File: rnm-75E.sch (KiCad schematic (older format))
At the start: 200 parts, among them J1 AVR-ISP-6, J2 USB_C_Receptacle_USB2.0, SW1 SW_Push, SW2 Rotary_Encoder_Switch, U1 AT90USB646-AU, U2 ATmega32U4-AU, Y1 Crystal_GND24_Small

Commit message: update mcu
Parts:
- removed U2: ATmega32U4-AU, Package_QFP:TQFP-44_10x10mm_P0.8mm, symbol MCU_Microchip_ATmega:ATmega32U4-AU
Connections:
- wire segments 419 -> 417
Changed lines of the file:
@@
 D+1
-$Comp
-L MCU_Microchip_ATmega:ATmega32U4-AU U2
-U 1 1 609C8DFF
-P 8750 4550
-F 0 "U2" H 8450 3950 50  0000 C CNN
-F 1 "ATmega32U4-AU" H 8650 3800 50  0000 C CNN
-F 2 "Package_QFP:TQFP-44_10x10mm_P0.8mm" H 8750 4550 50  0001 C CIN
-F 3 "http://ww1.microchip.com/downloads/en/DeviceDoc/Atmel-7766-8-bit-AVR-ATmega16U4-32U4_Datasheet.pdf" H 8750 4550 50  0001 C CNN
-	1    8750 4550
-	1    0    0    -1
-$EndComp
 $Comp
 L Device:R_Small R_u1
@@
 	1    0    0    -1
 $EndComp
-Wire Wire Line
-	7100 6200 6800 6200
 $Comp
 L power:GND #PWR0115
@@
 Text GLabel 3850 4800 2    50   Input ~ 0
 MOSI
-Wire Wire Line
-	6600 6200 6150 6200
 Text GLabel 3850 4900 2    50   Input ~ 0
 MISO

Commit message: pcb arranged
diodes added
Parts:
- added CAPS_LOCK_LED1: LED, LED_SMD:LED_0805_2012Metric, symbol Device:LED
- added D89, D90, D91, D92, D93, D94, D95, D96, D97, D98: WS2812B, LED_SMD:LED_WS2812B_PLCC4_5.0x5.0mm_P3.2mm, symbol LED:WS2812B
- added J3: Conn_01x04, Connector_PinSocket_2.54mm:PinSocket_1x04_P2.54mm_Vertical, symbol Connector_Generic:Conn_01x04
- added R1: 500, Resistor_SMD:R_0805_2012Metric, symbol Device:R_Small
- CF3, C_F1, C_F2, C_F4, C_FM1, C_X1, C_X2, C_ucap1: footprint (none) -> Capacitor_SMD:C_0805_2012Metric
- D1, D10, D11, D12, D13, D14, D15, D16, D17, D18, D19, D2, D20, D21, D22, D23, D24, D25, D26, D27, D28, D29, D3, D30, D31, D32, D33, D34, D35, D36, D37, D38, D39, D4, D40, D41, D42, D43, D44, D45, D46, D47, D48, D49, D5, D50, D51, D52, D53, D54, D55, D56, D57, D58, D59, D6, D60, D61, D62, D63, D64, D65, D66, D67, D68, D69, D7, D70, D71, D72, D73, D74, D75, D76, D77, D78, D79, D8, D80, D81, D82, D83, D84, D85, D86, D87, D88, D9: footprint (none) -> Diode_SMD:D_SOD-123
- F1: footprint (none) -> Fuse:Fuse_1206_3216Metric
- J1: footprint (none) -> Connector_PinSocket_1.00mm:PinSocket_2x03_P1.00mm_Vertical_SMD
- J2: footprint (none) -> Connector_USB:USB_C_Receptacle_HRO_TYPE-C-31-M-12
- MX1, MX12, MX13, MX15, MX16, MX17, MX18, MX19, MX2, MX21, MX22, MX23, MX24, MX25, MX26, MX27, MX28, MX29, MX3, MX30, MX31, MX32, MX33, MX34, MX35, MX36, MX37, MX38, MX39, MX4, MX40, MX42, MX43, MX44, MX45, MX46, MX47, MX48, MX49, MX5, MX50, MX51, MX52, MX53, MX54, MX55, MX56, MX57, MX58, MX59, MX6, MX60, MX61, MX62, MX63, MX65, MX66, MX67, MX68, MX69, MX7, MX70, MX72, MX73, MX74, MX75, MX76, MX78, MX79, MX83, MX84, MX85, MX86, MX87, MX88, MX89: footprint (none) -> MX_ONLY:MXOnly-1U-NoLED
- MX10, MX82: footprint (none) -> MX_ONLY:MXOnly-2.25U-NoLED
- MX11, MX14, MX20: footprint (none) -> MX_ONLY:MXOnly-1.25U-NoLED
- MX41: footprint (none) -> MX_ONLY:MXOnly-6.25U-ReversedStabilizers-NoLED
- MX64, MX71, MX8, MX81: footprint (none) -> MX_ONLY:MXOnly-1.5U-NoLED
- MX77, MX9: footprint (none) -> MX_ONLY:MXOnly-1.75U-NoLED
- MX80: footprint (none) -> MX_ONLY:MXOnly-2U-NoLED
- R_SW1, R_SW2, R_d1, R_d2, R_u1, R_u2: footprint (none) -> Resistor_SMD:R_0805_2012Metric
- SW1: footprint (none) -> random_keyboard_parts:SKQG-1155865
- SW2: footprint (none) -> Rotary_Encoder:RotaryEncoder_Alps_EC12E-Switch_Vertical_H20mm
- Y1: footprint (none) -> Crystal:Crystal_SMD_3225-4Pin_3.2x2.5mm
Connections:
- net +5V: now also SW2.A, SW2.B, U1.1 (PE6), U1.2 (PE7), D89.1 (VDD), D90.1 (VDD), D91.1 (VDD), D92.1 (VDD), D93.1 (VDD), D94.1 (VDD), D95.1 (VDD), D96.1 (VDD), D97.1 (VDD), D98.1 (VDD)
- net COL0: now also SW2.S1
- net COL10: no longer MX64.1 (COL)
- net COL15: no longer SW2.S1
- net COL7: now also U1.51 (PA0)
- net COL9: now also MX64.1 (COL)
- net GND: now also SW2.C, D89.3 (VSS), D90.3 (VSS), D91.3 (VSS), D92.3 (VSS), D93.3 (VSS), D94.3 (VSS), D95.3 (VSS), D96.3 (VSS), D97.3 (VSS), D98.3 (VSS), J3.4 (Pin_4), R1.2
- net ROWA: now also U1.32 (PD7); no longer U1.30 (PD5)
- net ROWB: now also U1.31 (PD6); no longer U1.29 (PD4)
- net ROWC: now also U1.30 (PD5); no longer U1.28 (PD3)
- net ROWD: now also U1.29 (PD4); no longer U1.27 (PD2)
- net ROWE: now also U1.28 (PD3); no longer U1.26 (PD1)
- net ROWF: now also U1.27 (PD2); no longer U1.25 (PD0)
- net VCC: now also J3.3 (Pin_3)
- net at D60.2 (A), MX63.2 (ROW): no longer MX64.2 (ROW)
- net at D53.2 (A), MX53.2 (ROW): now also MX64.2 (ROW)
- net LED_PIN: now reaches U1.10 (PB0)
- net LED_PIN: now also CAPS_LOCK_LED1.2 (A)
- net LED: now reaches U1.9 (PE3)
- net LED: now also D89.4 (DIN)
- new net: D89.2 (DOUT), D90.4 (DIN)
- new net: D90.2 (DOUT), D91.4 (DIN)
- new net: D91.2 (DOUT), D92.4 (DIN)
- new net: D92.2 (DOUT), D93.4 (DIN)
- new net: D93.2 (DOUT), D94.4 (DIN)
- new net: D94.2 (DOUT), D95.4 (DIN)
- new net: D95.2 (DOUT), D96.4 (DIN)
- new net: D96.2 (DOUT), D97.4 (DIN)
- new net: D97.2 (DOUT), D98.4 (DIN)
- new net: CAPS_LOCK_LED1.1 (K), R1.1
- new net SCL: J3.2 (Pin_2), U1.25 (PD0)
- new net SDA: J3.1 (Pin_1), U1.26 (PD1)
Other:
- note added: "LED TAP IN AFTER FUSE\n"
- moved on the sheet: D1, D10, D11, D12, D13, D14, D15, D16, D17, D18, D19, D2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

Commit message: stepped caps_lock
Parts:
- added MX90: MX-NoLED, MX_ONLY:MXOnly-1.25U-NoLED, symbol MX_ALPS_HYBRID:MX-NoLED
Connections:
- net COL1: now also MX90.1 (COL)
- net at D9.2 (A), MX9.2 (ROW): now also MX90.2 (ROW)
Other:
- note added: "ADD STEPPED CAPS SUPPORT\nUSES STEM PLACEMENT INLINE WITH L-CTRL\n"
- moved on the sheet: CAPS_LOCK_LED1, CF3, C_F1, C_F2, C_F4, C_FM1, C_X1, C_X2, C_ucap1, D1, D10, D11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

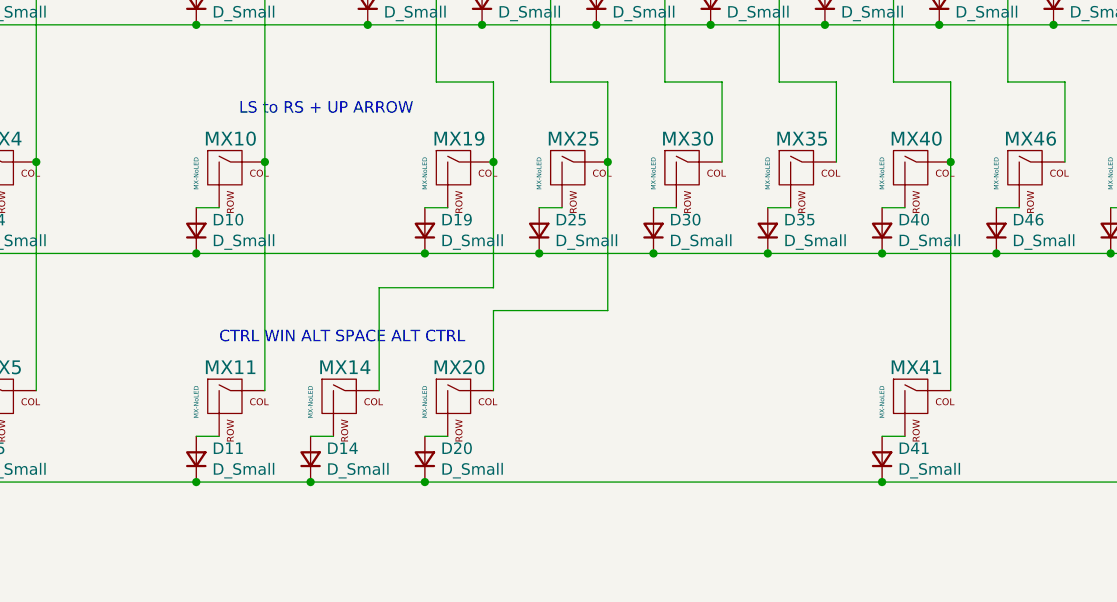
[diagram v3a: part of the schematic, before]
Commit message: added 7u space support
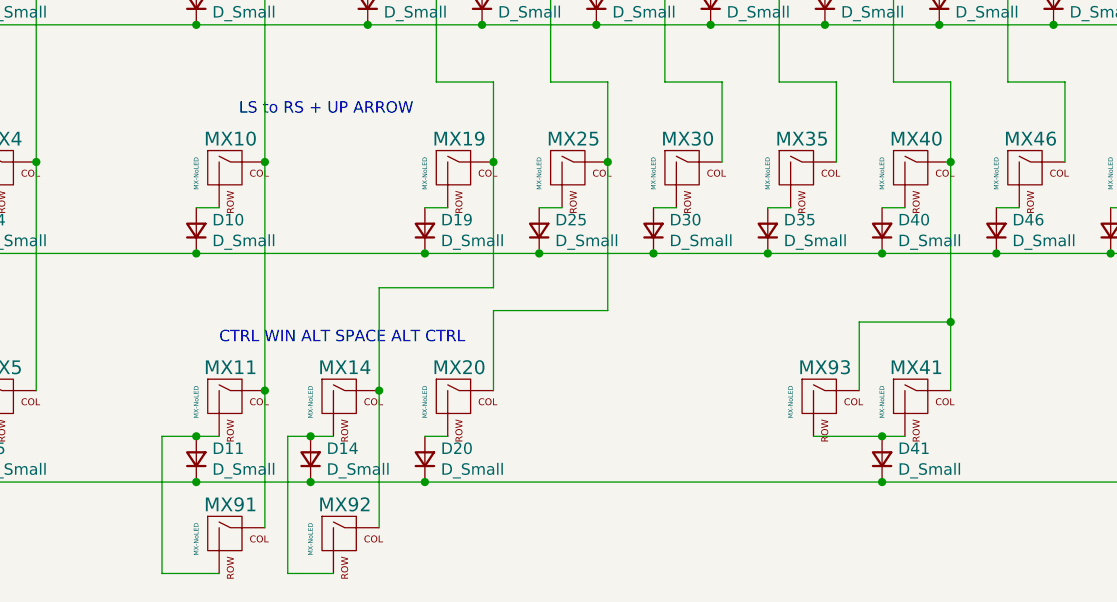
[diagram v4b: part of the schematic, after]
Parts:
- added MX91, MX92: MX-NoLED, MX_ONLY:MXOnly-1.5U-NoLED, symbol MX_ALPS_HYBRID:MX-NoLED
- added MX93: MX-NoLED, MX_ONLY:MXOnly-7U-ReversedStabilizers-NoLED, symbol MX_ALPS_HYBRID:MX-NoLED
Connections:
- net COL1: now also MX91.1 (COL)
- net COL2: now also MX92.1 (COL)
- net COL6: now also MX93.1 (COL)
- net at D11.2 (A), MX11.2 (ROW): now also MX91.2 (ROW)
- net at D14.2 (A), MX14.2 (ROW): now also MX92.2 (ROW)
- net at D41.2 (A), MX41.2 (ROW): now also MX93.2 (ROW)
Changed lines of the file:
@@
 Connection ~ 15900 8450
 Wire Wire Line
-	16150 9450 16150 10450
+	16150 9450 16150 10150
 Connection ~ 16150 9450
 Wire Wire Line
@@
 	12850 8600 12850 8650
 Connection ~ 12850 8650
+$Comp
+L MX_ALPS_HYBRID:MX-NoLED MX93
+U 1 1 60F4ECB9
+P 15600 10500
+F 0 "MX93" H 15600 10650 60  0000 C CNN
+F 1 "MX-NoLED" V 15450 10500 20  0000 C CNN
+F 2 "MX_ONLY:MXOnly-7U-ReversedStabilizers-NoLED" H 14975 10475 60  0001 C CNN
+F 3 "" H 14975 10475 60  0001 C CNN
+	1    15600 10500
+	1    0    0    -1
+$EndComp
+Wire Wire Line
+	15550 10650 15850 10650
+Connection ~ 15850 10650
+Wire Wire Line
+	15750 10450 15750 10150
+Wire Wire Line
+	15750 10150 16150 10150
+Connection ~ 16150 10150
+Wire Wire Line
+	16150 10150 16150 10450
+$Comp
+L MX_ALPS_HYBRID:MX-NoLED MX91
+U 1 1 60FCCE5A
+P 13000 11100
+F 0 "MX91" H 13000 11250 60  0000 C CNN
+F 1 "MX-NoLED" V 12850 11100 20  0000 C CNN
+F 2 "MX_ONLY:MXOnly-1.5U-NoLED" H 12375 11075 60  0001 C CNN
+F 3 "" H 12375 11075 60  0001 C CNN
+	1    13000 11100
+	1    0    0    -1
+$EndComp
+Wire Wire Line
+	12850 10650 12700 10650
+Wire Wire Line
+	12700 10650 12700 11250
+Wire Wire Line
+	12700 11250 12950 11250
+Connection ~ 12850 10650
+Wire Wire Line
+	13150 11050 13150 10450
+Connection ~ 13150 10450
+$Comp
+L MX_ALPS_HYBRID:MX-NoLED MX92
+U 1 1 6104E9AA
+P 13500 11100
+F 0 "MX92" H 13500 11250 60  0000 C CNN
+F 1 "MX-NoLED" V 13350 11100 20  0000 C CNN
+F 2 "MX_ONLY:MXOnly-1.5U-NoLED" H 12875 11075 60  0001 C CNN
+F 3 "" H 12875 11075 60  0001 C CNN
+	1    13500 11100
+	1    0    0    -1
+$EndComp
+Wire Wire Line
+	13450 11250 13250 11250
+Wire Wire Line
+	13250 11250 13250 10650
+Wire Wire Line
+	13250 10650 13350 10650
+Connection ~ 13350 10650
+Wire Wire Line
+	13650 11050 13650 10450
+Connection ~ 13650 10450
 $EndSCHEMATC

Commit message: wiring for row 1->4
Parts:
- added CAPS_LOCK_LED2: LED, LED_THT:LED_D3.0mm, symbol Device:LED
- CAPS_LOCK_LED1: footprint LED_SMD:LED_0805_2012Metric -> LED_THT:LED_D3.0mm
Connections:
- net +5V: no longer SW2.A, SW2.B, U1.1 (PE6), U1.2 (PE7)
- net LED_PIN: now also CAPS_LOCK_LED2.2 (A)
- net VCC: now also SW2.A, SW2.B, U1.1 (PE6), U1.2 (PE7)
- net at CAPS_LOCK_LED1.1 (K), R1.1: now also CAPS_LOCK_LED2.1 (K)
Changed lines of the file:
@@
 Text GLabel 4350 5050 0    50   Input ~ 0
 D-
-Text GLabel 3300 7100 0    50   Input ~ 0
-XTAL1
 $Comp
 L Device:Crystal_GND24_Small Y1
@@
 Wire Wire Line
 	6300 5300 6300 5600
-Text GLabel 7350 5100 2    50   Input ~ 0
-XTAL1
-Text GLabel 7350 5350 2    50   Input ~ 0
-XTAL2
 Wire Wire Line
 	6900 5300 6900 5350
@@
 Wire Wire Line
 	1650 8900 2150 8900
-Text GLabel 3300 7300 0    50   Input ~ 0
-XTAL2
 Text GLabel 3300 6900 0    50   Input ~ 0
 RESET
@@
 Text GLabel 10700 4550 0    50   Input ~ 0
 ENCODER_B
-$Comp
-L power:+5V #PWR0119
-U 1 1 61C5F900
-P 11150 3900
-F 0 "#PWR0119" H 11150 3750 50  0001 C CNN
-F 1 "+5V" H 11165 4073 50  0000 C CNN
-F 2 "" H 11150 3900 50  0001 C CNN
-F 3 "" H 11150 3900 50  0001 C CNN
-	1    11150 3900
-	1    0    0    -1
-$EndComp
-$Comp
-L power:+5V #PWR0120
-U 1 1 61C6148D
-P 12350 3900
-F 0 "#PWR0120" H 12350 3750 50  0001 C CNN
-F 1 "+5V" H 12365 4073 50  0000 C CNN
-F 2 "" H 12350 3900 50  0001 C CNN
-F 3 "" H 12350 3900 50  0001 C CNN
-	1    12350 3900
-	1    0    0    -1
-$EndComp
 Wire Wire Line
 	10700 4550 11150 4550
@@
 F 0 "CAPS_LOCK_LED1" H 18493 3845 50  0000 C CNN
 F 1 "LED" H 18493 3936 50  0000 C CNN
-F 2 "LED_SMD:LED_0805_2012Metric" H 18500 4100 50  0001 C CNN
+F 2 "LED_THT:LED_D3.0mm" H 18500 4100 50  0001 C CNN
 F 3 "~" H 18500 4100 50  0001 C CNN
 	1    18500 4100
 	-1   0    0    1
 $EndComp
-Text GLabel 18350 4100 0    50   Input ~ 0
+Text GLabel 17950 4100 0    50   Input ~ 0
 LED_PIN
 $Comp
@@
 	1    0    0    -1
 $EndComp
-Wire Wire Line
-	18650 4100 19000 4100
 $Comp
 L Device:R_Small R1
@@
 	13650 11050 13650 10450
 Connection ~ 13650 10450
+$Comp
+L Device:LED CAPS_LOCK_LED2
+U 1 1 60A1F01D
+P 18500 4450
+F 0 "CAPS_LOCK_LED2" H 18493 4195 50  0000 C CNN
+F 1 "LED" H 18493 4286 50  0000 C CNN
+F 2 "LED_THT:LED_D3.0mm" H 18500 4450 50  0001 C CNN
+F 3 "~" H 18500 4450 50  0001 C CNN
+	1    18500 4450
+	-1   0    0    1
+$EndComp
+Wire Wire Line
+	17950 4100 18100 4100
+Wire Wire Line
+	18100 4100 18100 4450
+Wire Wire Line
+	18100 4450 18350 4450
+Connection ~ 18100 4100
+Wire Wire Line
+	18100 4100 18350 4100
+Text GLabel 7350 5350 2    50   Input ~ 0
+XTAL2
+Text GLabel 7350 5100 2    50   Input ~ 0
+XTAL1
+Text GLabel 3300 7300 0    50   Input ~ 0
+XTAL2
+Wire Wire Line
+	18650 4450 18850 4450
+Wire Wire Line
+	18850 4450 18850 4100
+Wire Wire Line
+	18650 4100 18850 4100
+Wire Wire Line
+	18850 4100 19000 4100
+Connection ~ 18850 4100
+Text GLabel 3300 7100 0    50   Input ~ 0
+XTAL1
+$Comp
+L power:VCC #PWR?
+U 1 1 60C2D023
+P 11350 3900
+F 0 "#PWR?" H 11350 3750 50  0001 C CNN
+F 1 "VCC" H 11365 4073 50  0000 C CNN
+F 2 "" H 11350 3900 50  0001 C CNN
+F 3 "" H 11350 3900 50  0001 C CNN
+	1    11350 3900
+	1    0    0    -1
+$EndComp
+$Comp
+L power:VCC #PWR?
+U 1 1 60C2DEE9
+P 12200 3900
+F 0 "#PWR?" H 12200 3750 50  0001 C CNN
+F 1 "VCC" H 12215 4073 50  0000 C CNN
+F 2 "" H 12200 3900 50  0001 C CNN
+F 3 "" H 12200 3900 50  0001 C CNN
+	1    12200 3900
+	1    0    0    -1
+$EndComp
+Wire Wire Line
+	11150 3900 11350 3900
+Wire Wire Line
+	12200 3900 12350 3900
 $EndSCHEMATC

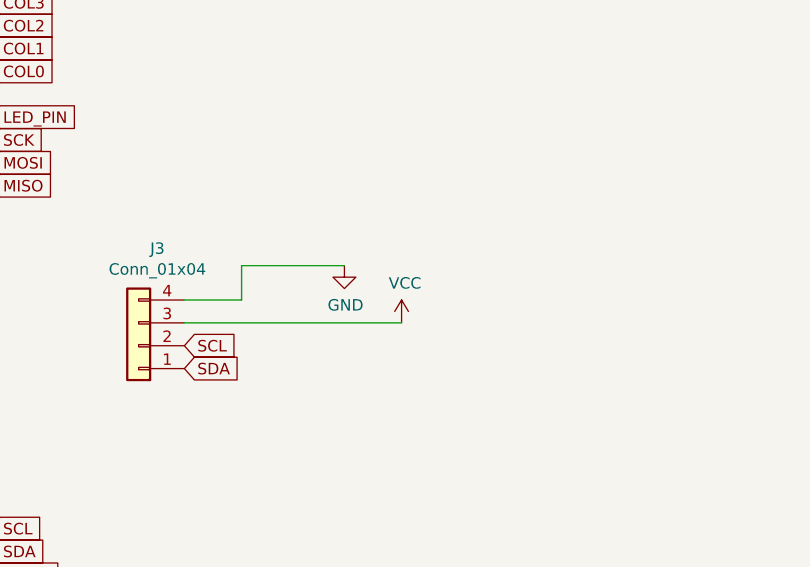
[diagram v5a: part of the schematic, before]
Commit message: route scl/sda
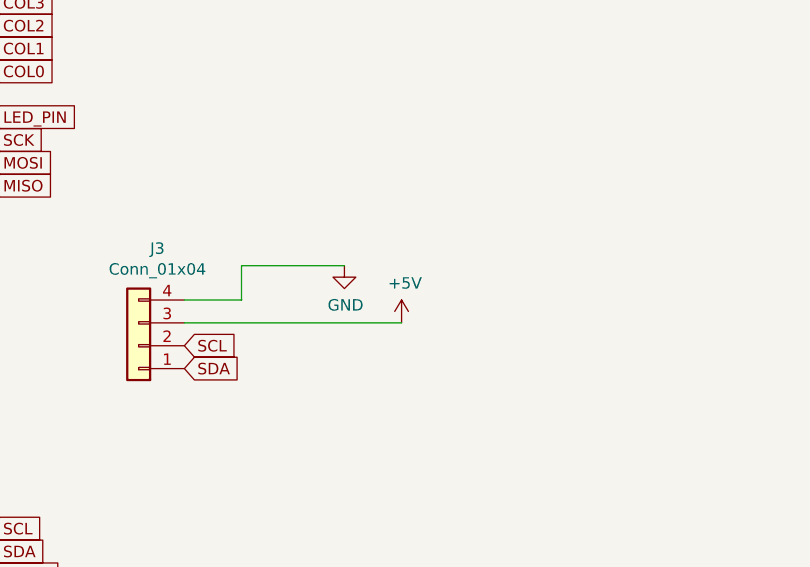
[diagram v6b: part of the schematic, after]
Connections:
- net +5V: now also J3.3 (Pin_3)
- net VCC: no longer J3.3 (Pin_3)
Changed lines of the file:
@@
 Wire Wire Line
 	5600 8450 6050 8450
-$Comp
-L power:VCC #PWR0125
-U 1 1 6285CCAE
-P 6300 8700
-F 0 "#PWR0125" H 6300 8550 50  0001 C CNN
-F 1 "VCC" H 6315 8873 50  0000 C CNN
-F 2 "" H 6300 8700 50  0001 C CNN
-F 3 "" H 6300 8700 50  0001 C CNN
-	1    6300 8700
-	1    0    0    -1
-$EndComp
 Wire Wire Line
 	5350 8700 6300 8700
@@
 XTAL1
 $Comp
-L power:VCC #PWR?
+L power:VCC #PWR0119
 U 1 1 60C2D023
 P 11350 3900
-F 0 "#PWR?" H 11350 3750 50  0001 C CNN
+F 0 "#PWR0119" H 11350 3750 50  0001 C CNN
 F 1 "VCC" H 11365 4073 50  0000 C CNN
 F 2 "" H 11350 3900 50  0001 C CNN
@@
 $EndComp
 $Comp
-L power:VCC #PWR?
+L power:VCC #PWR0120
 U 1 1 60C2DEE9
 P 12200 3900
-F 0 "#PWR?" H 12200 3750 50  0001 C CNN
+F 0 "#PWR0120" H 12200 3750 50  0001 C CNN
 F 1 "VCC" H 12215 4073 50  0000 C CNN
 F 2 "" H 12200 3900 50  0001 C CNN
@@
 Wire Wire Line
 	12200 3900 12350 3900
+$Comp
+L power:+5V #PWR?
+U 1 1 60E1267F
+P 6300 8700
+F 0 "#PWR?" H 6300 8550 50  0001 C CNN
+F 1 "+5V" H 6315 8873 50  0000 C CNN
+F 2 "" H 6300 8700 50  0001 C CNN
+F 3 "" H 6300 8700 50  0001 C CNN
+	1    6300 8700
+	1    0    0    -1
+$EndComp
 $EndSCHEMATC

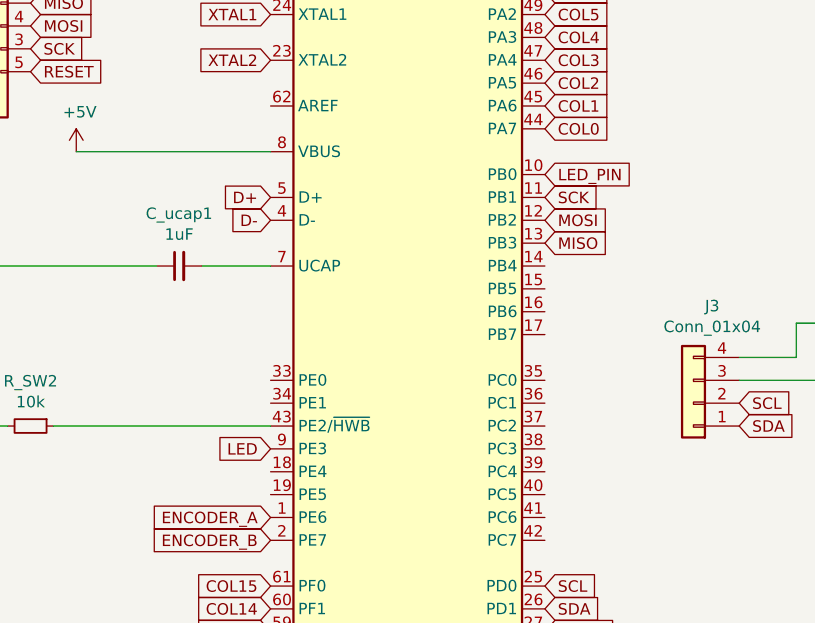
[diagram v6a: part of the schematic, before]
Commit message: WIRED SPI
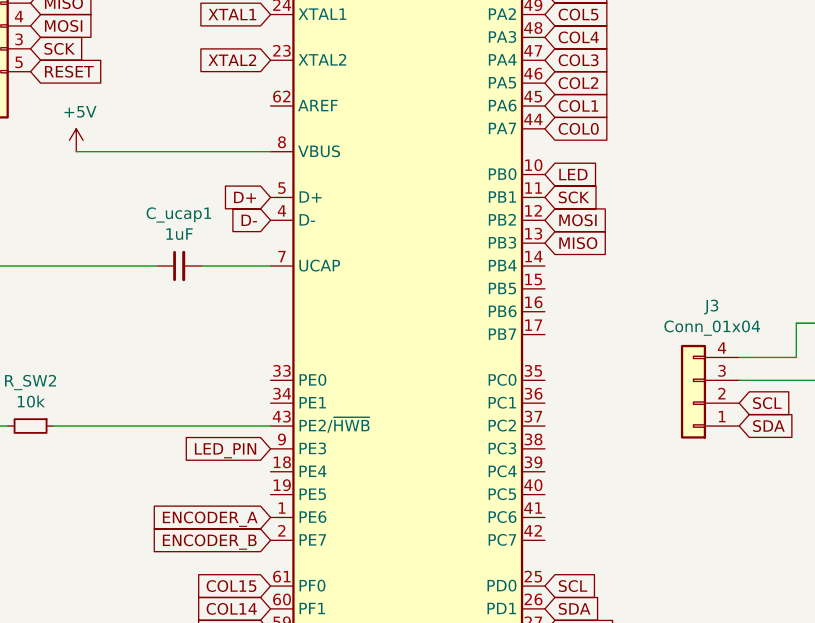
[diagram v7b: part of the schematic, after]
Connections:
- net LED: now also U1.10 (PB0); no longer U1.9 (PE3)
- net LED_PIN: now also U1.9 (PE3); no longer U1.10 (PB0)
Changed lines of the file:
@@
 Wire Wire Line
 	18350 2850 18750 2850
-Text GLabel 3300 9000 0    50   Input ~ 0
+Text GLabel 4500 7800 2    50   Input ~ 0
 LED
 Text GLabel 9600 2850 0    50   Input ~ 0
@@
 Text GLabel 5350 8900 2    50   Input ~ 0
 SDA
-Text GLabel 4500 7800 2    50   Input ~ 0
+Text GLabel 3300 9000 0    50   Input ~ 0
 LED_PIN
 Text GLabel 4500 9800 2    50   Input ~ 0
@@
 	12200 3900 12350 3900
 $Comp
-L power:+5V #PWR?
+L power:+5V #PWR0125
 U 1 1 60E1267F
 P 6300 8700
-F 0 "#PWR?" H 6300 8550 50  0001 C CNN
+F 0 "#PWR0125" H 6300 8550 50  0001 C CNN
 F 1 "+5V" H 6315 8873 50  0000 C CNN
 F 2 "" H 6300 8700 50  0001 C CNN
